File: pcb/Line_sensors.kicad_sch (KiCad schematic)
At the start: 28 parts, among them U10 CNY70, U11 CNY70, U5 CNY70, U6 CNY70, U7 CNY70, U8 CNY70, U9 CNY70

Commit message: [pcb] BT config rework
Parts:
- renumbered U11 to U10, U5 to U4, U6 to U5, U7 to U6, U8 to U7, U9 to U8, U10 to U9

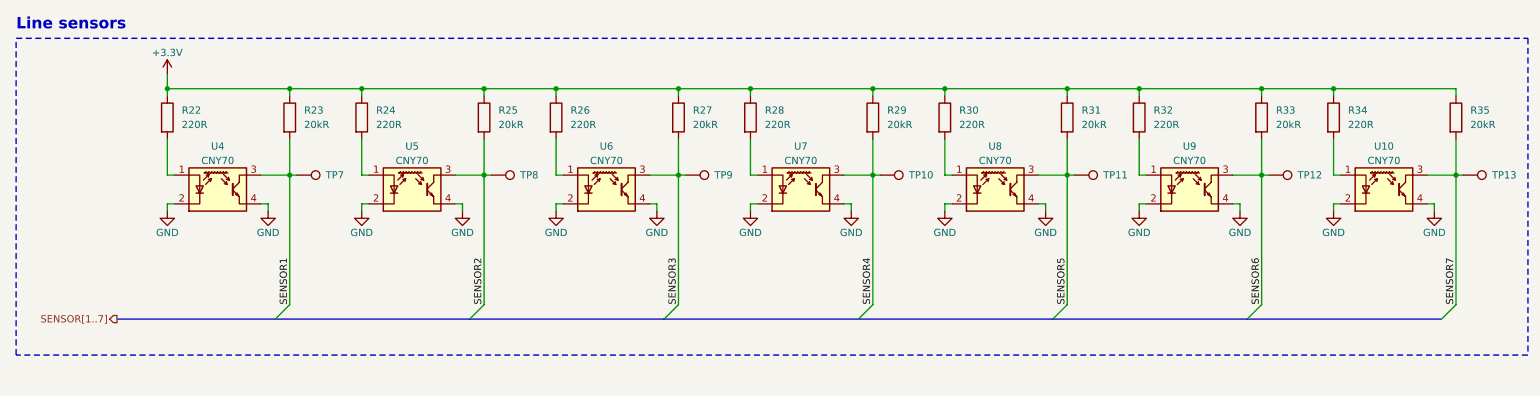
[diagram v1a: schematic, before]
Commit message: [pcb] More final touches, UART test ponts added.
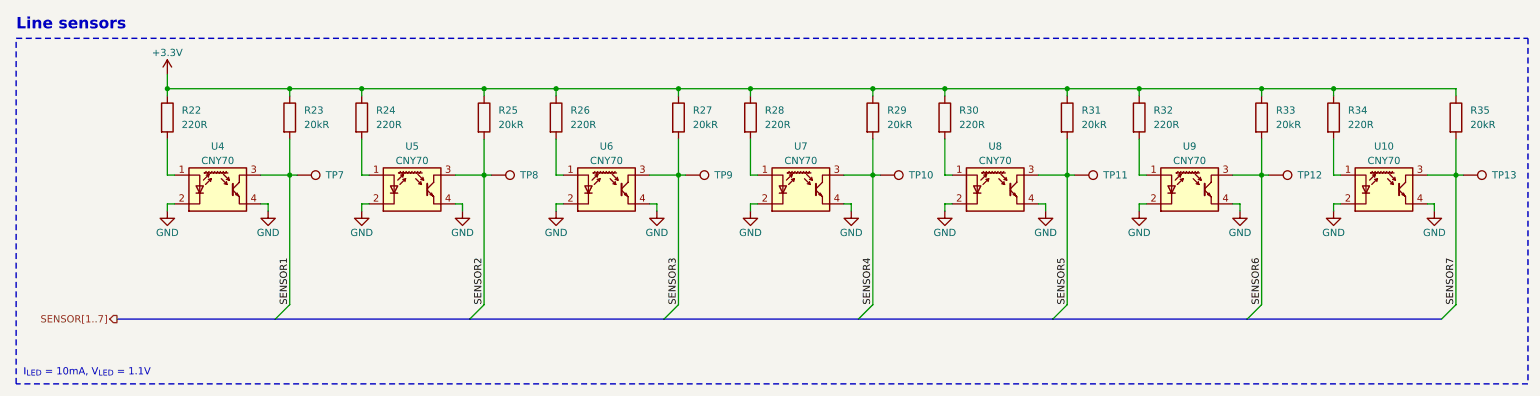
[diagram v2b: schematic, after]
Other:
- note added: "I_{LED} = 10mA, V_{LED} = 1.1V"
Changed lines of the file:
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@@
     (stroke (width 0) (type default))
   )
-  (rectangle (start 15.24 19.05) (end 281.94 74.93)
+  (rectangle (start 15.24 19.05) (end 281.94 80.01)
     (stroke (width 0.25) (type dash))
     (fill (type none))
   )
+  (text "I_{LED} = 10mA, V_{LED} = 1.1V" (at 16.51 78.74 0)
+    (effects (font (size 1.27 1.27)) (justify left bottom))
+  )
   (text "Line sensors" (at 15.24 17.78 0)

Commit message: [pcb] ERC/DRC checks
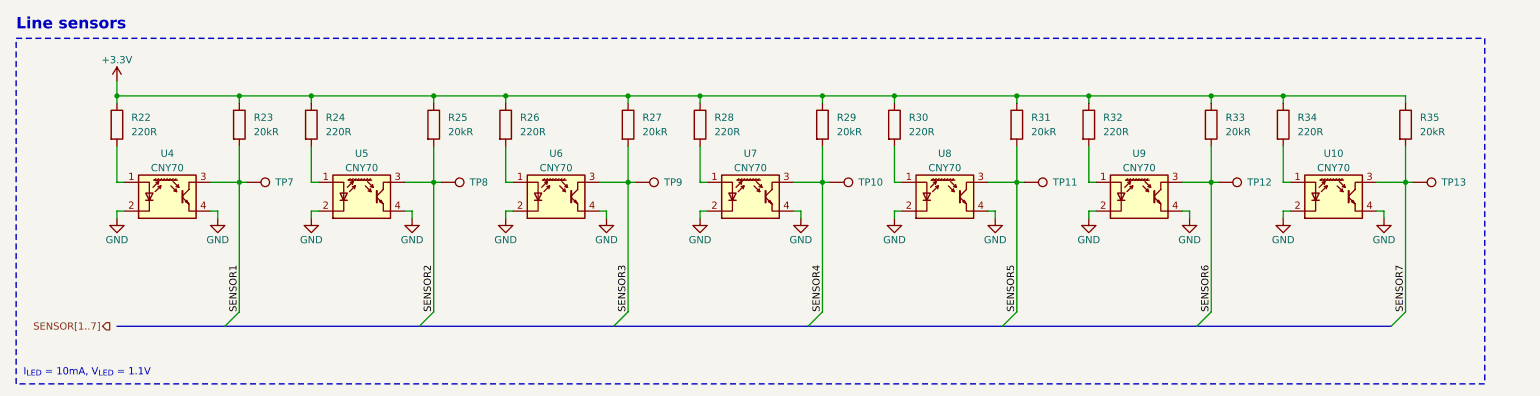
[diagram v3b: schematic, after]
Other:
- moved on the sheet: R22, R23, R24, R25, R26, R27, R28, R29, R30, R31, R32, R33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
